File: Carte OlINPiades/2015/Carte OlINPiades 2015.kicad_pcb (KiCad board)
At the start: 2 copper layers, 0 parts

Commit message: ajouté pcb
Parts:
- added Batteries1: CONN_2, Connect:bornier2, F.Cu at (148.5, 105.0)
- added C1, C5, C6: 100nF, Capacitors_SMD:C_0805_HandSoldering, F.Cu at (148.5, 105.0)
- added C2, C7: 10uF, Capacitors_SMD:C_0805_HandSoldering, F.Cu at (148.5, 105.0)
- added C3: 15pF, Capacitors_SMD:C_0805_HandSoldering, F.Cu at (148.5, 105.0)
- added C4: 330nF, Capacitors_SMD:C_0805_HandSoldering, F.Cu at (148.5, 105.0)
- added D1, D10, D100, D101, D102, D103, D104, D105, D106, D107, D108, D109, D11, D110, D111, D112, D113, D114, D115, D116, D117, D118, D119, D12, D120, D121, D122, D123, D124, D125, D126, D127, D128, D129, D13, D130, D131, D132, D133, D134, D135, D136, D137, D138, D139, D14, D140, D141, D142, D143, D144, D145, D146, D147, D148, D149, D15, D150, D151, D152, D153, D154, D155, D156, D157, D158, D159, D16, D160, D161, D162, D163, D164, D165, D166, D167, D168, D169, D17, D170, D171, D172, D173, D174, D175, D176, D177, D178, D179, D18, D180, D181, D182, D183, D184, D185, D186, D187, D188, D189, D19, D190, D191, D192, D193, D194, D195, D196, D197, D198, D199, D2, D20, D200, D201, D202, D203, D204, D205, D206, D207, D208, D209, D21, D210, D211, D212, D213, D214, D215, D216, D217, D218, D219, D22, D220, D221, D222, D223, D224, D225, D226, D227, D228, D229, D23, D230, D231, D232, D233, D234, D235, D236, D237, D238, D239, D24, D240, D241, D242, D243, D244, D245, D246, D247, D248, D249, D25, D250, D251, D252, D253, D254, D255, D256, D26, D27, D28, D29, D3, D30, D31, D32, D33, D34, D35, D36, D37, D38, D39, D4, D40, D41, D42, D43, D44, D45, D46, D47, D48, D49, D5, D50, D51, D52, D53, D54, D55, D56, D57, D58, D59, D6, D60, D61, D62, D63, D64, D65, D66, D67, D68, D69, D7, D70, D71, D72, D73, D74, D75, D76, D77, D78, D79, D8, D80, D81, D82, D83, D84, D85, D86, D87, D88, D89, D9, D90, D91, D92, D93, D94, D95, D96, D97, D98, D99: LED, LEDs:LED-3MM, F.Cu at (148.5, 105.0)
- added DEMUX1: 74HC4067, Housings_SOIC:SOIC-24_7.5x15.4mm_Pitch1.27mm, F.Cu at (148.5, 105.0)
- added Pickit1: CONN_5, Pin_Headers:Pin_Header_Straight_1x05, F.Cu at (148.5, 105.0)
- added R1: 10kOhm, Resistors_SMD:R_0805_HandSoldering, F.Cu at (148.5, 105.0)
- added R2: 470Ohm, Resistors_SMD:R_0805_HandSoldering, F.Cu at (148.5, 105.0)
- added R3: TODO, Resistors_SMD:R_0805_HandSoldering, F.Cu at (148.5, 105.0)
- added S1: CAT4016, Housings_SOIC:SOIC-24_7.5x15.4mm_Pitch1.27mm, F.Cu at (148.5, 105.0)
- added S2, S3, S4, S5, S6, S7, S8, S9: TPS2080, Housings_SOIC:SOIC-8_3.9x4.9mm_Pitch1.27mm, F.Cu at (148.5, 105.0)
- added U1: dsPIC33FJ128MC802, Housings_SOIC:SOIC-28_7.5x17.9mm_Pitch1.27mm, F.Cu at (148.5, 105.0)
- added U2: LM7805, Transistors_SMD:sot428, F.Cu at (148.5, 105.0)
- added U3: LM2937-3.3, Transistors_SMD:sot428, F.Cu at (148.5, 105.0)
- added UART1, UART2: CONN_2, Pin_Headers:Pin_Header_Straight_1x02, F.Cu at (148.5, 105.0)

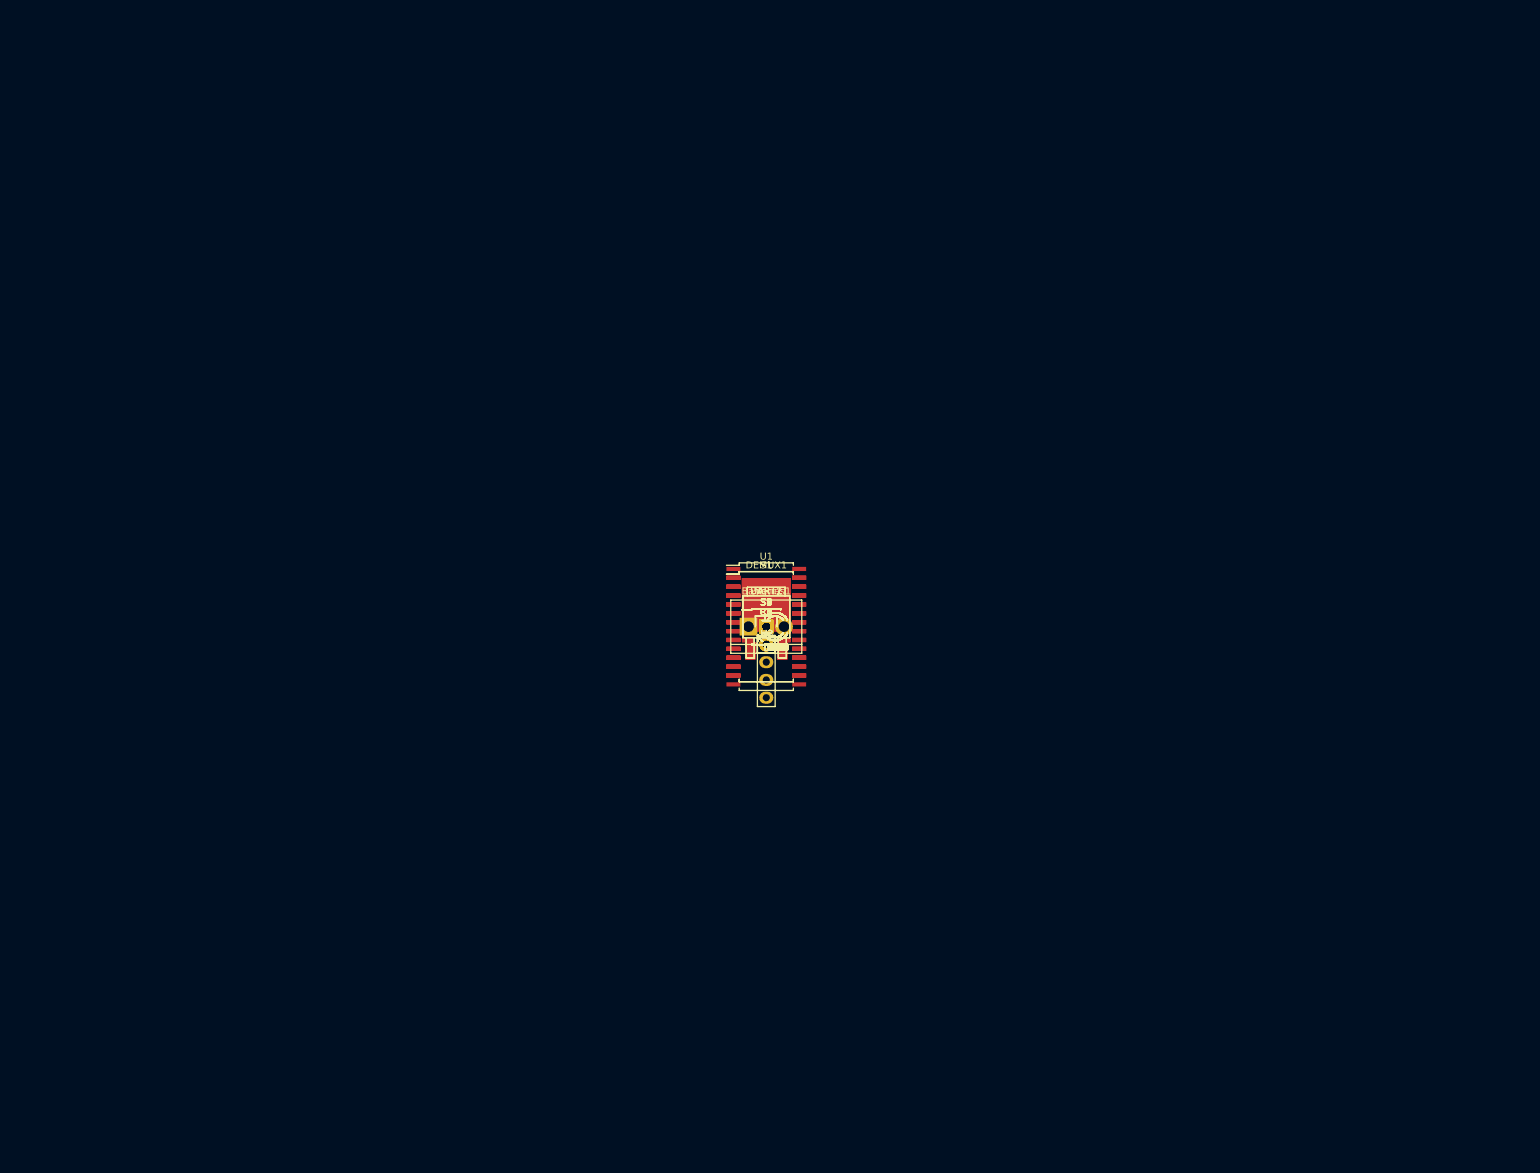
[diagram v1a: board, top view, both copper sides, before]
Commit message: séparation composants
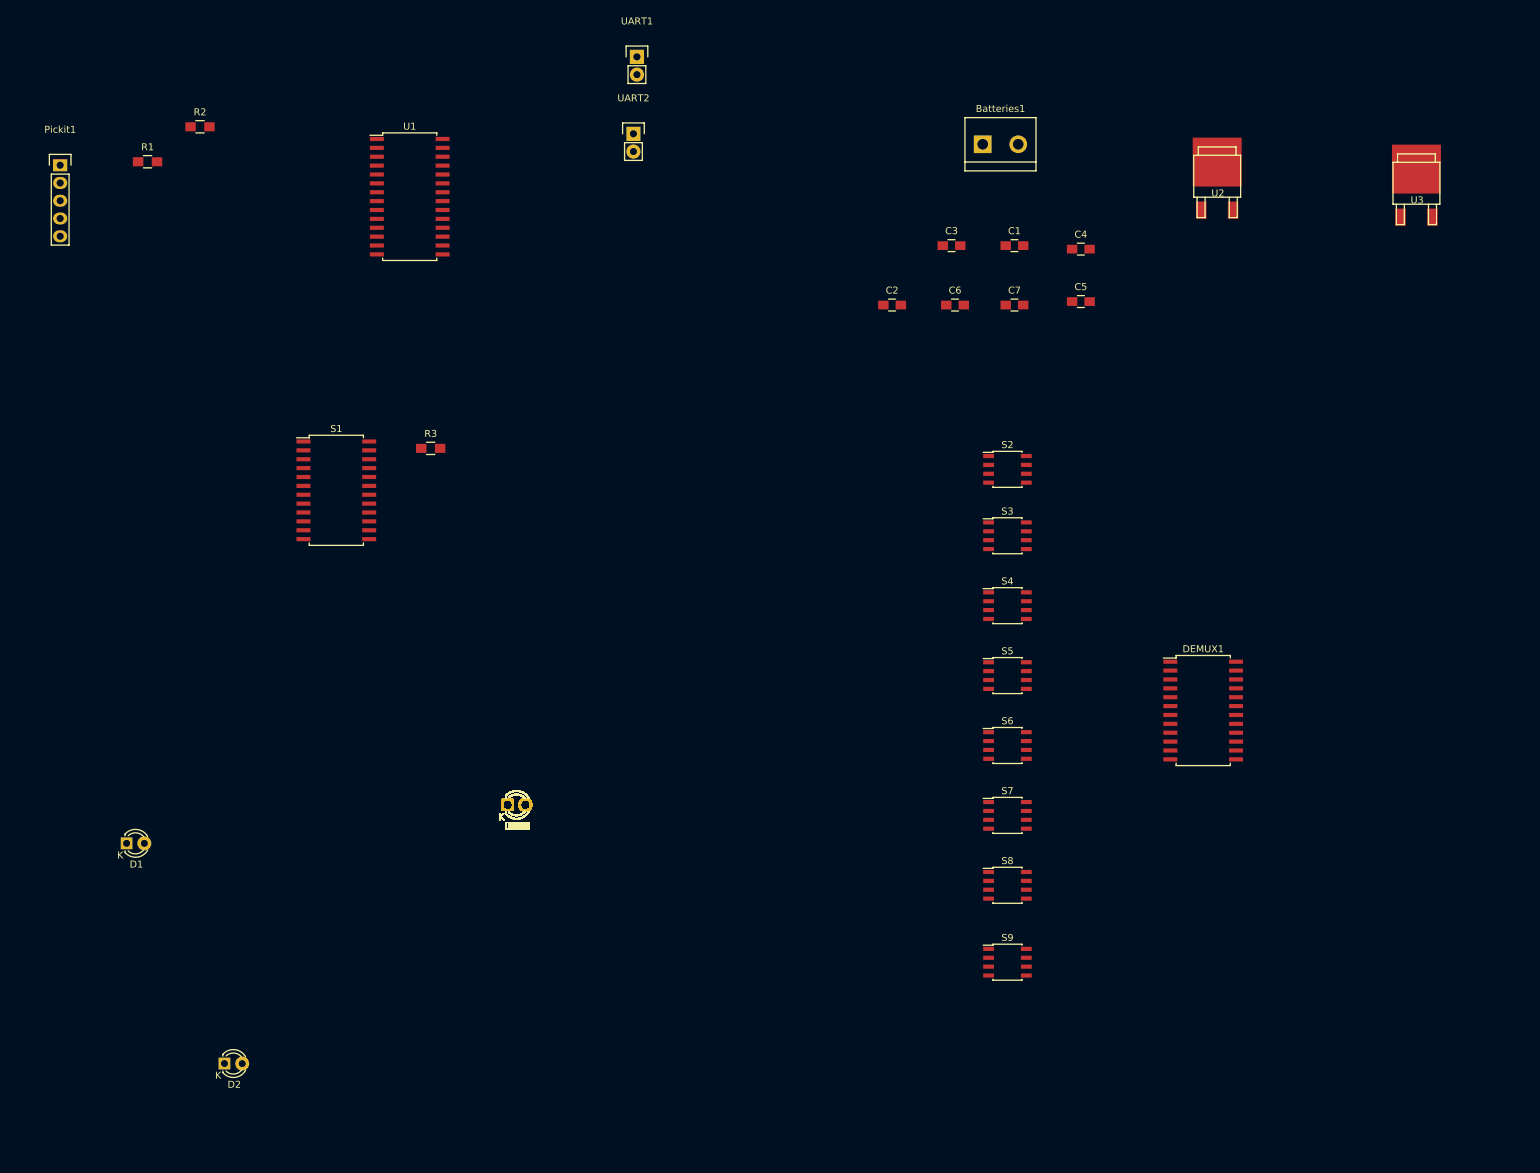
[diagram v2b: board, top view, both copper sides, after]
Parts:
- moved Pickit1 120.7 mm to (47.5, 39.0)
- moved U3 111.8 mm to (241.5, 43.0)
- moved R1 110.7 mm to (60.0, 38.5)
- moved R2 108.0 mm to (67.5, 33.5)
- moved D2 99.6 mm to (71.0, 167.5)
- moved D1 96.6 mm to (57.0, 136.0)
- moved U2 90.2 mm to (213.0, 42.0)
- moved UART1 83.6 mm to (130.0, 23.5)
- moved U1 79.9 mm to (97.5, 43.5)
- moved Batteries1 76.7 mm to (182.0, 36.0)
- moved UART2 73.0 mm to (129.5, 34.5)
- moved C4 70.3 mm to (193.5, 51.0)
- moved C1 65.0 mm to (184.0, 50.5)
- moved C5 64.7 mm to (193.5, 58.5)
- moved S1 64.5 mm to (87.0, 85.5)
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
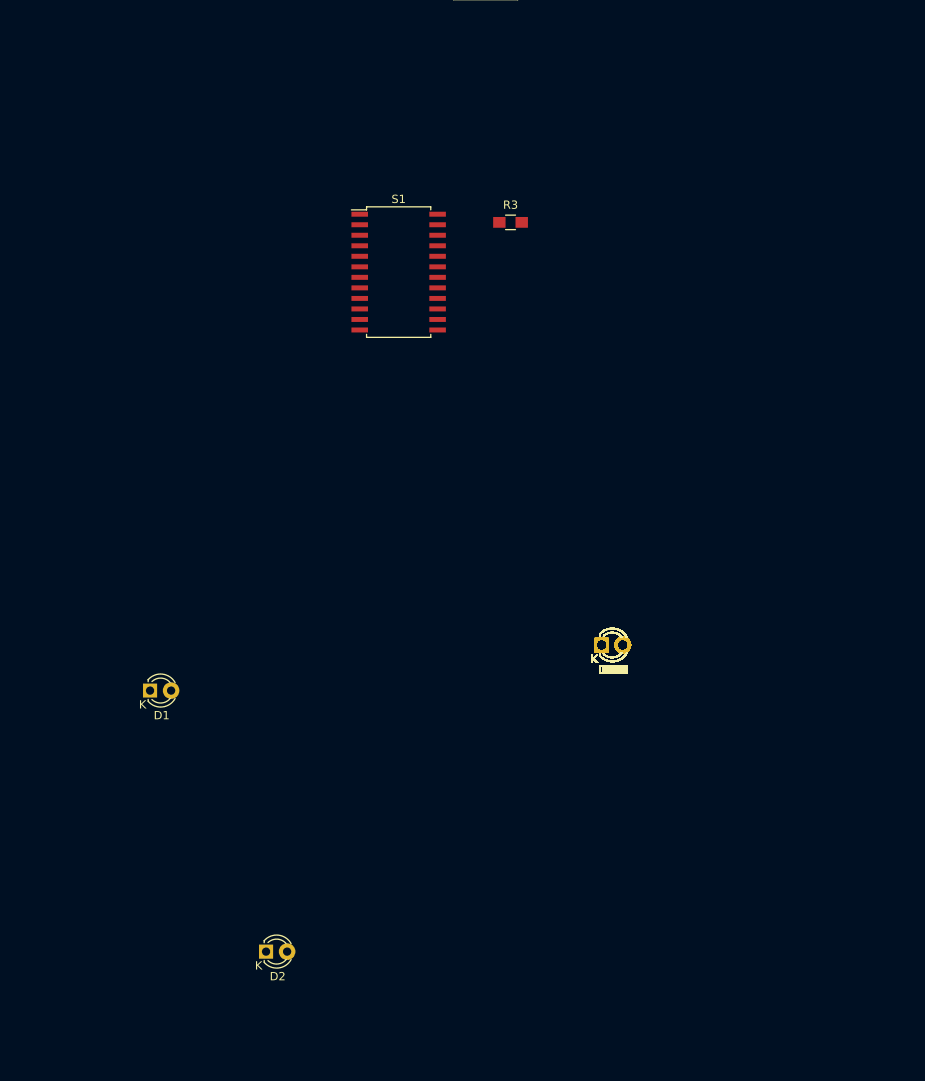
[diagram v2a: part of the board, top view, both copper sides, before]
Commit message: placement des leds
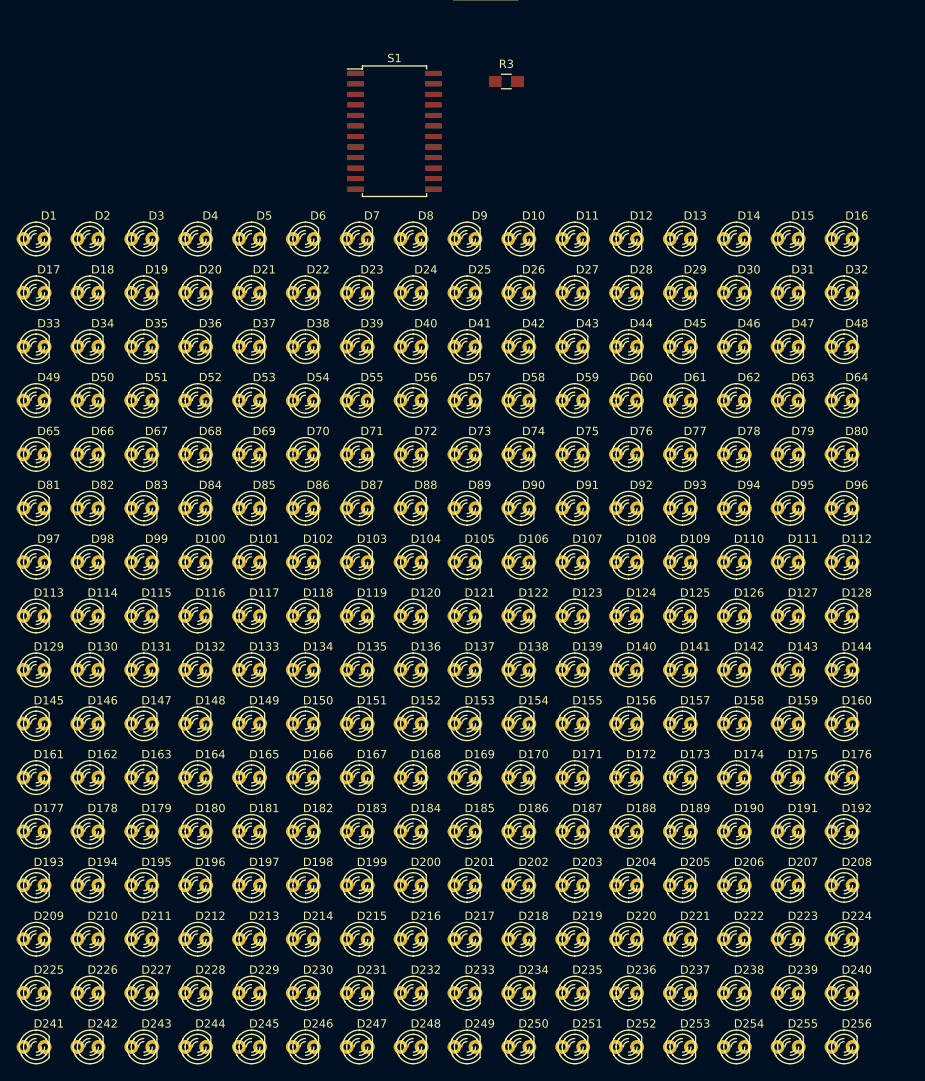
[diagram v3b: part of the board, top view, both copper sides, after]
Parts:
- moved D2 88.6 mm to (49.5, 81.5)
- moved D241 83.9 mm to (43.0, 179.0)
- moved D17 80.6 mm to (43.0, 88.0)
- moved D225 80.3 mm to (43.0, 172.5)
- moved D242 78.7 mm to (49.5, 179.0)
- moved D33 77.4 mm to (43.0, 94.5)
- moved D209 77.2 mm to (43.0, 166.0)
- moved D18 75.2 mm to (49.5, 88.0)
- moved D226 74.9 mm to (49.5, 172.5)
- moved D49 74.6 mm to (43.0, 101.0)
- moved D193 74.4 mm to (43.0, 159.5)
- moved D3 74.0 mm to (56.0, 81.5)
- moved D243 73.7 mm to (56.0, 179.0)
- moved D65 72.3 mm to (43.0, 107.5)
- moved D177 72.1 mm to (43.0, 153.0)
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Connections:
- net VCC renamed +3.3V
- net VPP renamed +5V

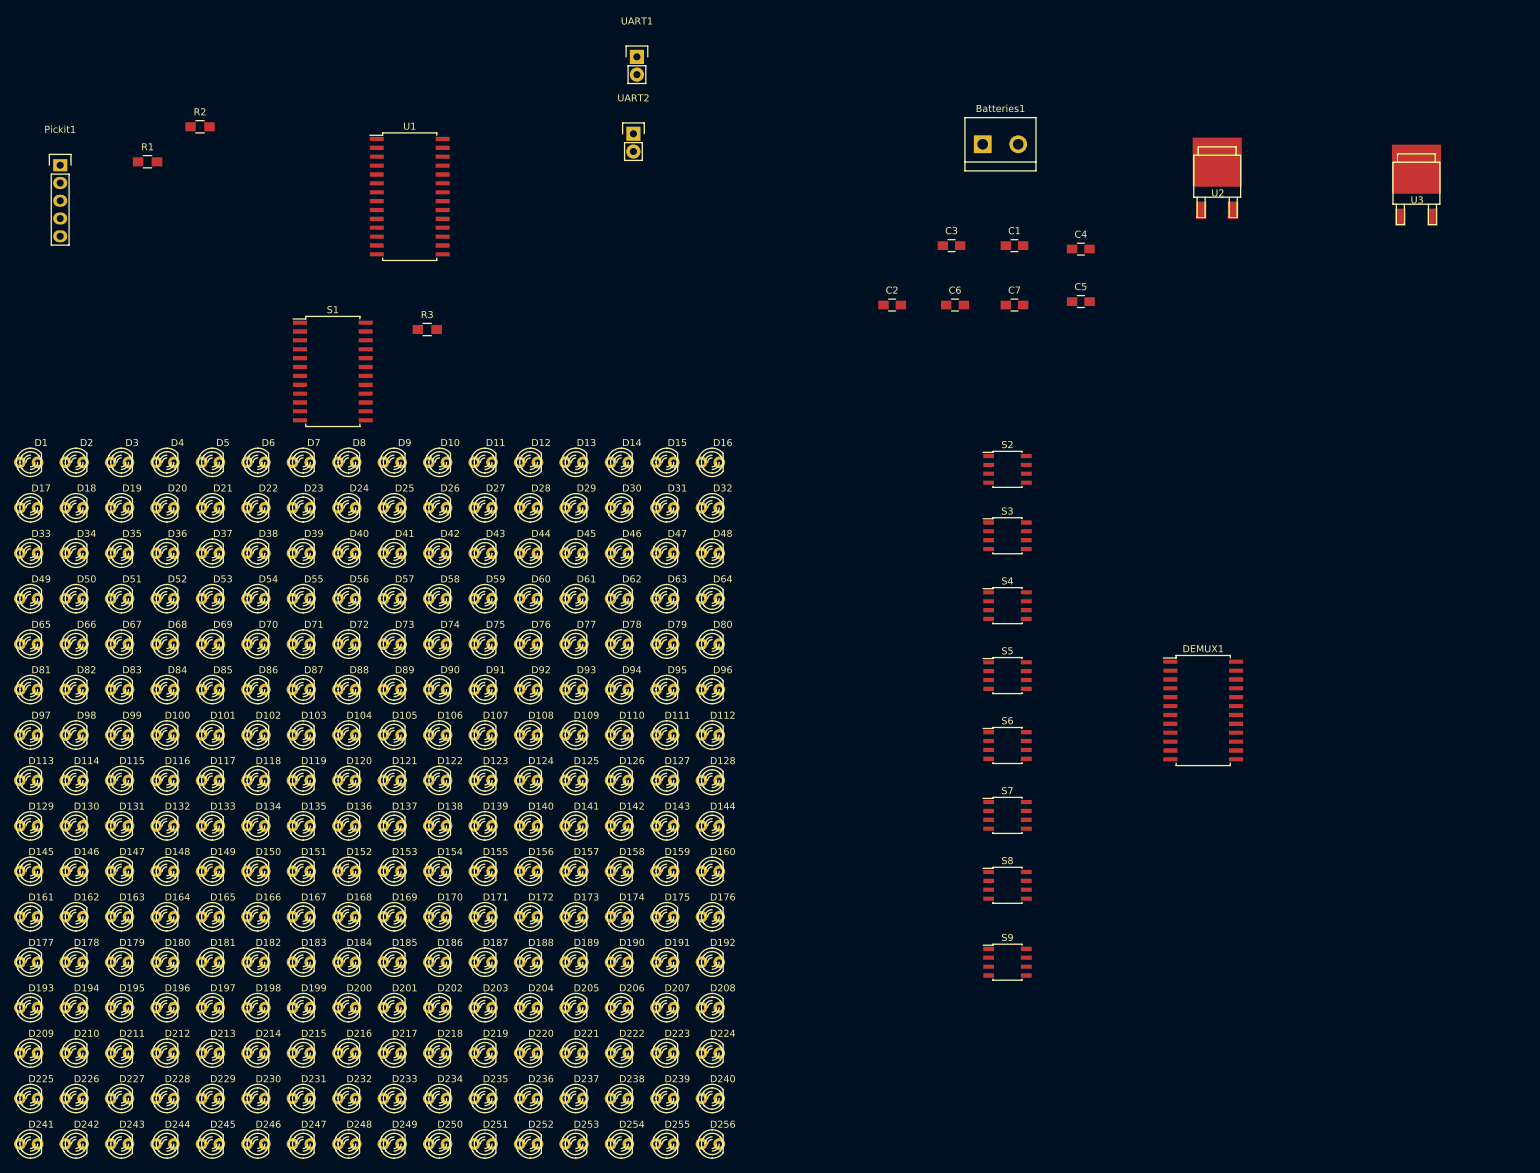
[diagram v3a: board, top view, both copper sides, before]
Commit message: proposition placement composants
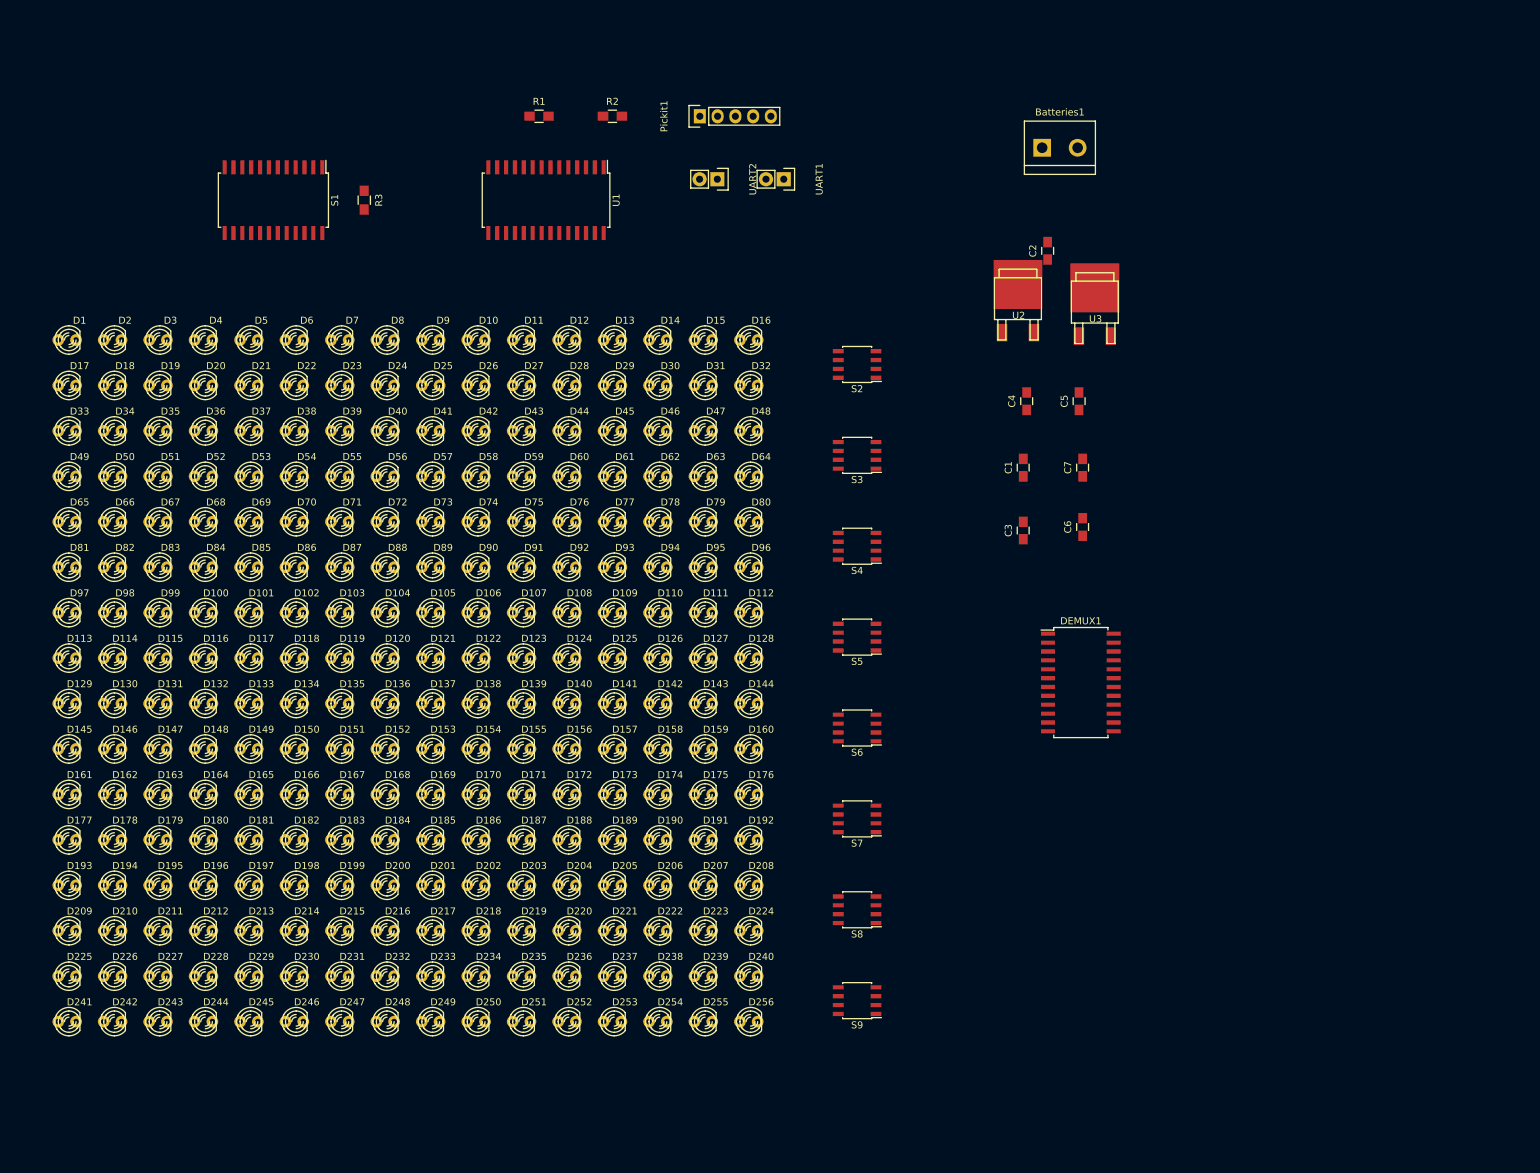
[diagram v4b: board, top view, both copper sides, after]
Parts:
- moved Pickit1 91.8 mm to (139.0, 32.0), turned to 90 degrees
- moved R2 59.0 mm to (126.5, 32.0)
- moved R1 56.4 mm to (116.0, 32.0)
- moved U3 49.0 mm to (195.5, 60.0)
- moved C3 42.0 mm to (185.2, 91.2), turned to 90 degrees
- moved C6 36.6 mm to (193.8, 90.8), turned to 90 degrees
- moved U2 33.4 mm to (184.5, 59.5)
- moved C1 31.8 mm to (185.2, 82.2), turned to 90 degrees
- moved UART1 27.3 mm to (151.0, 41.0), turned to 270 degrees
- moved S2 26.2 mm to (161.5, 67.5), turned to 180 degrees
- moved S1 25.9 mm to (78.0, 44.0), turned to 270 degrees
- moved C7 25.2 mm to (193.8, 82.2), turned to 90 degrees
- moved S3 24.4 mm to (161.5, 80.5), turned to 180 degrees
- moved C2 23.6 mm to (188.8, 51.2), turned to 90 degrees
- moved S4 23.1 mm to (161.5, 93.5), turned to 180 degrees
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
